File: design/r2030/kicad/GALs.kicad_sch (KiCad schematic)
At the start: 12 parts, among them IC2 ATF22V10C, IC3 ATF22V10C, IC5 ATF22V10C, IC6 ATF22V10C

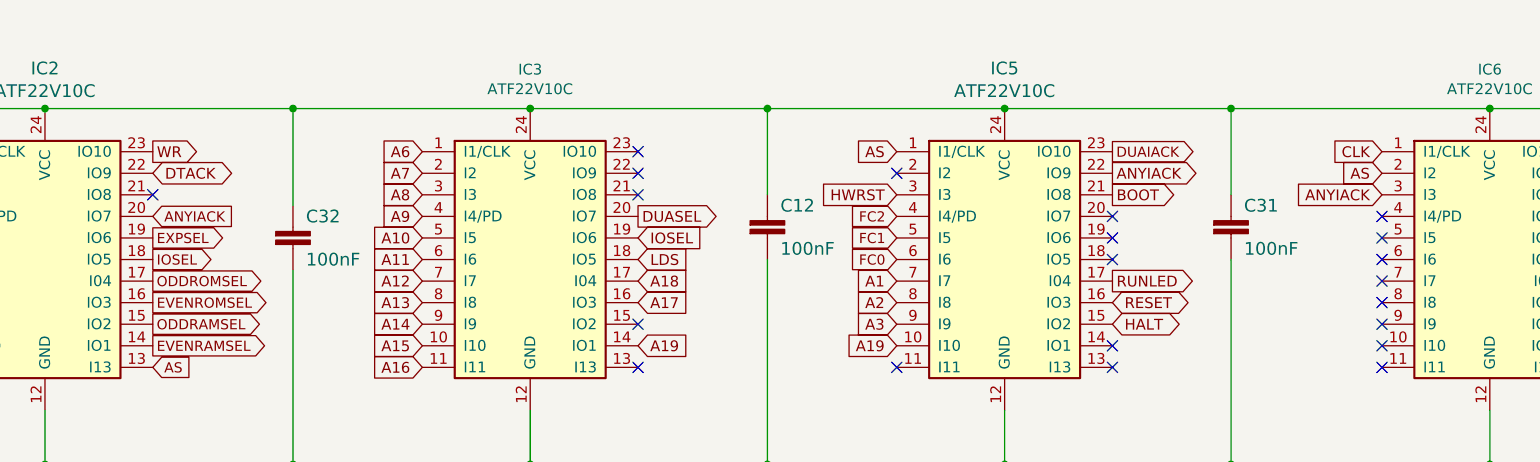
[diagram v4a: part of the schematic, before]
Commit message: Feature/smd birdseed (#427)
* GAL changes to better support coprocessor

* Update designs for copro GAL change

* Revert accidental DUARTSEL changes

* Re-add mistakenly-removed polarity symbols

* Tentative r2 SMD design

* Resize tiny resistors

* More address lines into GALs

* Reroute for FTDI

* prod

* Correct FT2232HL part number

* Mask expansion and silk tidy after first spin
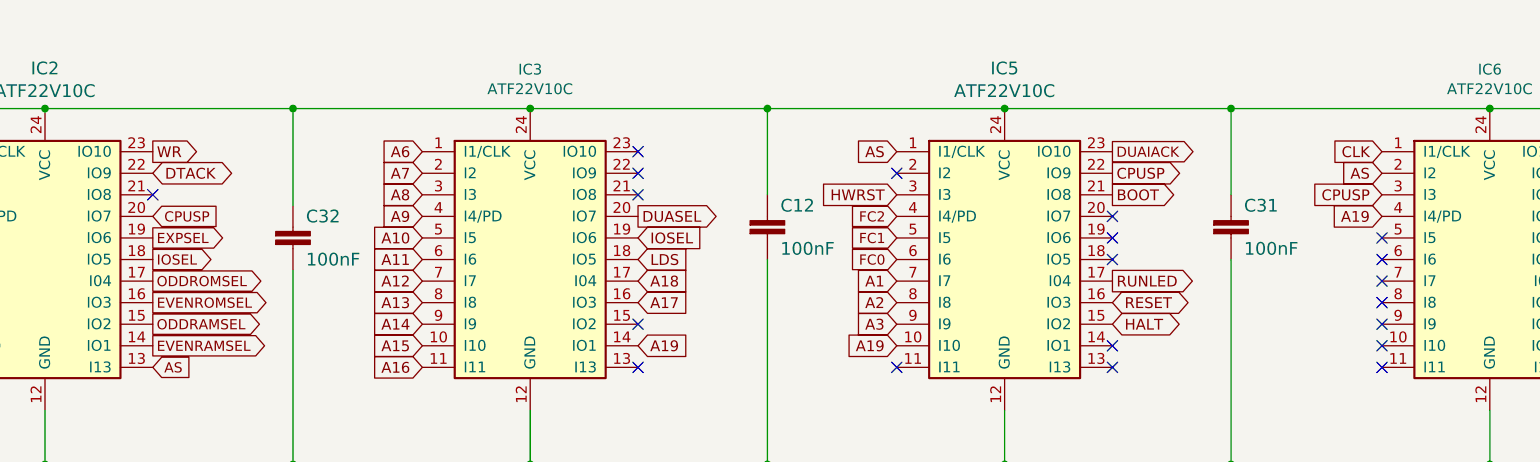
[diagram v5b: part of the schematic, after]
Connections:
- net A19: now also IC6.4 (I4/PD)
- net ANYIACK renamed CPUSP
- no-connect marks 30 -> 29
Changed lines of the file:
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@@
   (title_block
     (title "ROSCO_M68K CLASSIC MC68030 EDITION")
-    (date "2024-03-09")
+    (date "2024-03-17")
     (rev "2.10")
     (company "The Really Old-School Company Limited")
@@
   )
   (no_connect (at 133.35 88.9))
-  (no_connect (at 220.98 93.98))
   (no_connect (at 133.35 91.44))
   (no_connect (at 133.35 106.68))
@@
     )
   )
+  (global_label "A19" (shape input) (at 220.98 93.98 180) (fields_autoplaced)
+    (effects (font (size 1.27 1.27)) (justify right))
+    (property "Intersheetrefs" "${INTERSHEET_REFS}" (at 215.1414 93.98 0)
+      (effects (font (size 1.27 1.27)) (justify right) hide)
+    )
+  )
   (global_label "LDS" (shape input) (at 50.8 104.14 180) (fields_autoplaced)
     (effects (font (size 1.1938 1.1938)) (justify right))
@@
     )
   )
-  (global_label "ANYIACK" (shape input) (at 220.98 91.44 180) (fields_autoplaced)
-    (effects (font (size 1.27 1.27)) (justify right))
-    (property "Intersheetrefs" "${INTERSHEET_REFS}" (at 0 0 0)
-      (effects (font (size 1.27 1.27)) hide)
+  (global_label "CPUSP" (shape input) (at 220.98 91.44 180) (fields_autoplaced)
+    (effects (font (size 1.27 1.27)) (justify right))
+    (property "Intersheetrefs" "${INTERSHEET_REFS}" (at 212.299 91.44 0)
+      (effects (font (size 1.27 1.27)) (justify right) hide)
     )
   )
@@
     )
   )
-  (global_label "ANYIACK" (shape input) (at 76.2 93.98 0) (fields_autoplaced)
+  (global_label "CPUSP" (shape input) (at 76.2 93.98 0) (fields_autoplaced)
     (effects (font (size 1.1938 1.1938)) (justify left))
-    (property "Intersheetrefs" "${INTERSHEET_REFS}" (at 0 0 0)
-      (effects (font (size 1.27 1.27)) hide)
+    (property "Intersheetrefs" "${INTERSHEET_REFS}" (at 84.3599 93.98 0)
+      (effects (font (size 1.27 1.27)) (justify left) hide)
     )
   )
@@
     )
   )
-  (global_label "ANYIACK" (shape output) (at 189.23 88.9 0) (fields_autoplaced)
-    (effects (font (size 1.27 1.27)) (justify left))
-    (property "Intersheetrefs" "${INTERSHEET_REFS}" (at 0 0 0)
-      (effects (font (size 1.27 1.27)) hide)
-    )
-  )
+  (global_label "CPUSP" (shape output) (at 189.23 88.9 0) (fields_autoplaced)
+    (effects (font (size 1.27 1.27)) (justify left))
+    (property "Intersheetrefs" "${INTERSHEET_REFS}" (at 197.911 88.9 0)
+      (effects (font (size 1.27 1.27)) (justify left) hide)
+    )
+  )
